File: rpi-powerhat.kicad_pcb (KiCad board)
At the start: 2 copper layers, 65 x 56 mm, 5 parts, among them J2 rpi-gpio-powerhat

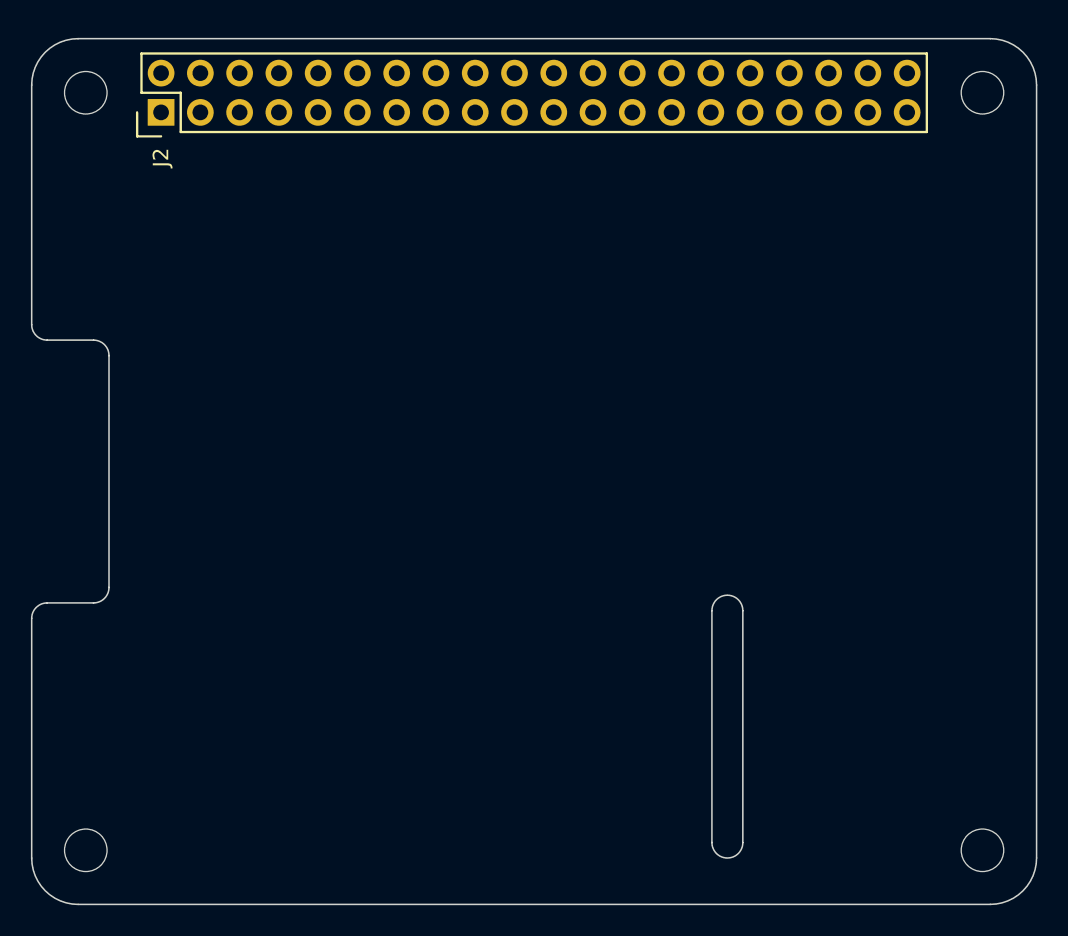
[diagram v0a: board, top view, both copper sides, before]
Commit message: Made the powerhat even smaller
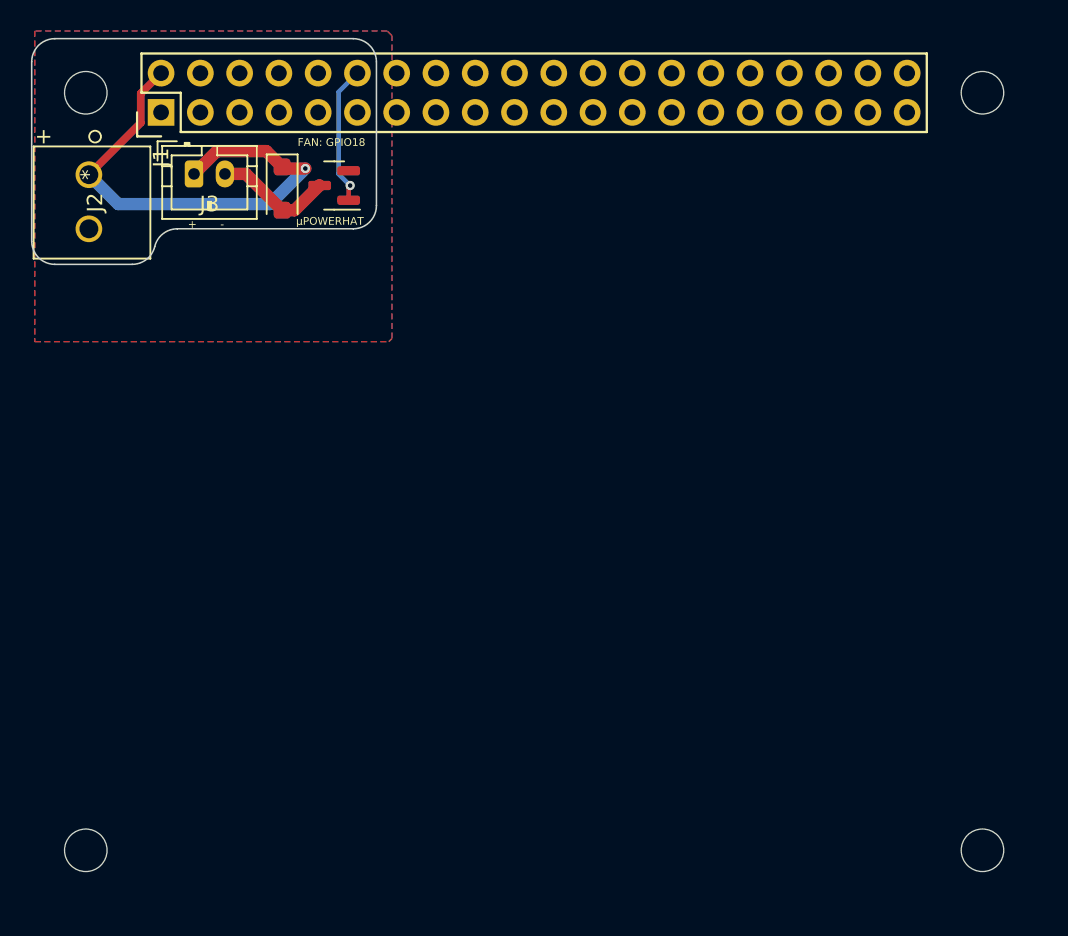
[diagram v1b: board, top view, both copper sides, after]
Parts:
- added D1: D, Diode_SMD:D_SOD-123F, F.Cu at (16.2, 10.2)
- added J2: +5V, rpi-powerhat:1546551-2, F.Cu at (3.70, 9.30)
- added J3: FAN, Connector_JST:JST_PH_B2B-PH-K_1x02_P2.00mm_Vertical, F.Cu at (10.5, 9.25)
- added Q2: AO3402, Package_TO_SOT_SMD:SOT-23, F.Cu at (19.6, 10.0)
- J1: renamed from J2; footprint RPi_Hat:Pin_Header_Straight_2x20 -> rpi-powerhat:Pin_Header_Straight_2x20
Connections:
- J1 pad 1: Net-(J2-Pad1) -> unconnected-(J1-3.3V-Pad1)
- J1 pad 10: Net-(J2-Pad10) -> unconnected-(J1-BCM15_RXD-Pad10)
- J1 pad 11: Net-(J2-Pad11) -> unconnected-(J1-BCM17-Pad11)
- J1 pad 12: Net-(J2-Pad12) -> GPIO18
- J1 pad 13: Net-(J2-Pad13) -> unconnected-(J1-BCM27-Pad13)
- J1 pad 14: Net-(J2-Pad14) -> unconnected-(J1-GND-Pad14)
- J1 pad 15: Net-(J2-Pad15) -> unconnected-(J1-BCM22-Pad15)
- J1 pad 16: Net-(J2-Pad16) -> unconnected-(J1-BCM23-Pad16)
- J1 pad 17: Net-(J2-Pad17) -> unconnected-(J1-3.3V-Pad17)
- J1 pad 18: Net-(J2-Pad18) -> unconnected-(J1-BCM24-Pad18)
- J1 pad 19: Net-(J2-Pad19) -> unconnected-(J1-BCM10_MOSI-Pad19)
- J1 pad 2: Net-(J2-Pad2) -> +5V
- J1 pad 20: Net-(J2-Pad20) -> unconnected-(J1-GND-Pad20)
- J1 pad 21: Net-(J2-Pad21) -> unconnected-(J1-BCM9_MISO-Pad21)
- J1 pad 22: Net-(J2-Pad22) -> unconnected-(J1-BCM25-Pad22)
- J1 pad 23: Net-(J2-Pad23) -> unconnected-(J1-BCM11_SCLK-Pad23)
- J1 pad 24: Net-(J2-Pad24) -> unconnected-(J1-BCM8_CE0-Pad24)
- J1 pad 25: Net-(J2-Pad25) -> unconnected-(J1-GND-Pad25)
- J1 pad 26: Net-(J2-Pad26) -> unconnected-(J1-BCM7_CE1-Pad26)
- J1 pad 27: Net-(J2-Pad27) -> unconnected-(J1-BCM0_ID_SD-Pad27)
- J1 pad 28: Net-(J2-Pad28) -> unconnected-(J1-BCM1_ID_SC-Pad28)
- J1 pad 29: Net-(J2-Pad29) -> unconnected-(J1-BCM5-Pad29)
- J1 pad 3: Net-(J2-Pad3) -> unconnected-(J1-BCM2_SDA-Pad3)
- J1 pad 30: Net-(J2-Pad30) -> unconnected-(J1-GND-Pad30)
- J1 pad 31: Net-(J2-Pad31) -> unconnected-(J1-BCM6-Pad31)
- J1 pad 32: Net-(J2-Pad32) -> unconnected-(J1-BCM12_PWM0-Pad32)
- J1 pad 33: Net-(J2-Pad33) -> unconnected-(J1-BCM13_PWM1-Pad33)
- J1 pad 34: Net-(J2-Pad34) -> unconnected-(J1-GND-Pad34)
- J1 pad 35: Net-(J2-Pad35) -> unconnected-(J1-BCM19_MISO_PCM_FS-Pad35)
- J1 pad 36: Net-(J2-Pad36) -> unconnected-(J1-BCM16-Pad36)
- J1 pad 37: Net-(J2-Pad37) -> unconnected-(J1-BCM26-Pad37)
- J1 pad 38: Net-(J2-Pad38) -> unconnected-(J1-BCM20_MOSI_PCM_DI-Pad38)
- J1 pad 39: Net-(J2-Pad39) -> unconnected-(J1-GND-Pad39)
- J1 pad 4: Net-(J2-Pad4) -> unconnected-(J1-5V-Pad4)
- J1 pad 40: Net-(J2-Pad40) -> unconnected-(J1-BCM21_SCLK_PCM_DO-Pad40)
- J1 pad 5: Net-(J2-Pad5) -> unconnected-(J1-BCM3_SCL-Pad5)
- J1 pad 6: Net-(J2-Pad6) -> unconnected-(J1-GND-Pad6)
- J1 pad 7: Net-(J2-Pad7) -> unconnected-(J1-BCM4_GPCLK0-Pad7)
- J1 pad 8: Net-(J2-Pad8) -> unconnected-(J1-BCM14_TXD-Pad8)
- J1 pad 9: Net-(J2-Pad9) -> GND
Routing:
- net +5V: track 0.00 -> 32.5 mm, vias 0 -> 1
- net GPIO18: track 0.00 -> 9.07 mm, vias 0 -> 1
- net /rpi-gpio-powerhat/GPIO18-: track 0.00 -> 7.70 mm
- added copper zone on B.Cu, net GND
- added copper zone on F.Cu, net GND
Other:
- board size 65 x 56 mm -> 22.3 x 14.6 mm
- board text added: "+"
- board text added: "-"
- board text added: "FAN: GPIO18"
- board text added: "GND"
- board text added: "µPOWERHAT"
- board text removed: "Camera Flex Slot (Optional)"

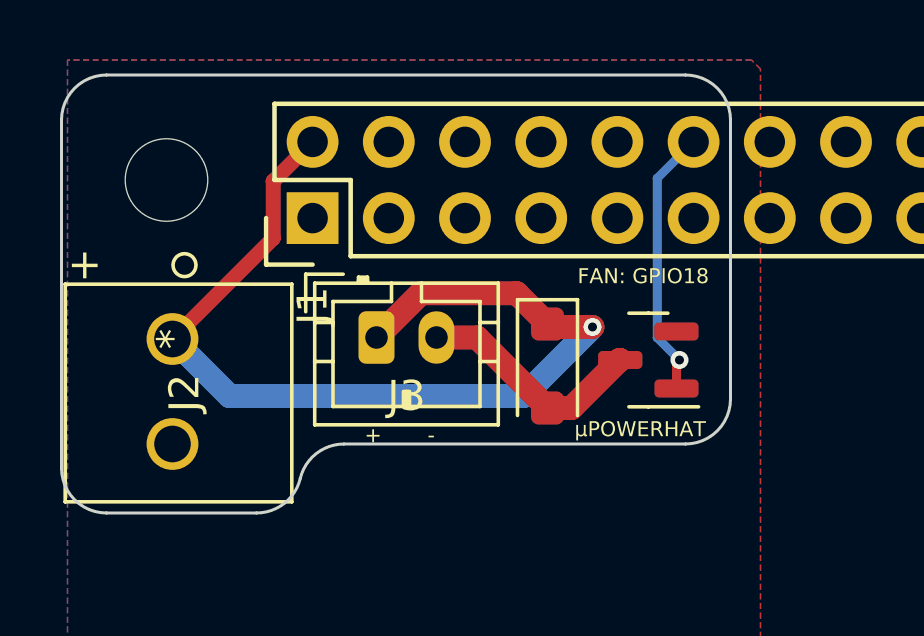
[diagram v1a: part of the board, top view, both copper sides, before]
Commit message: Added more vias
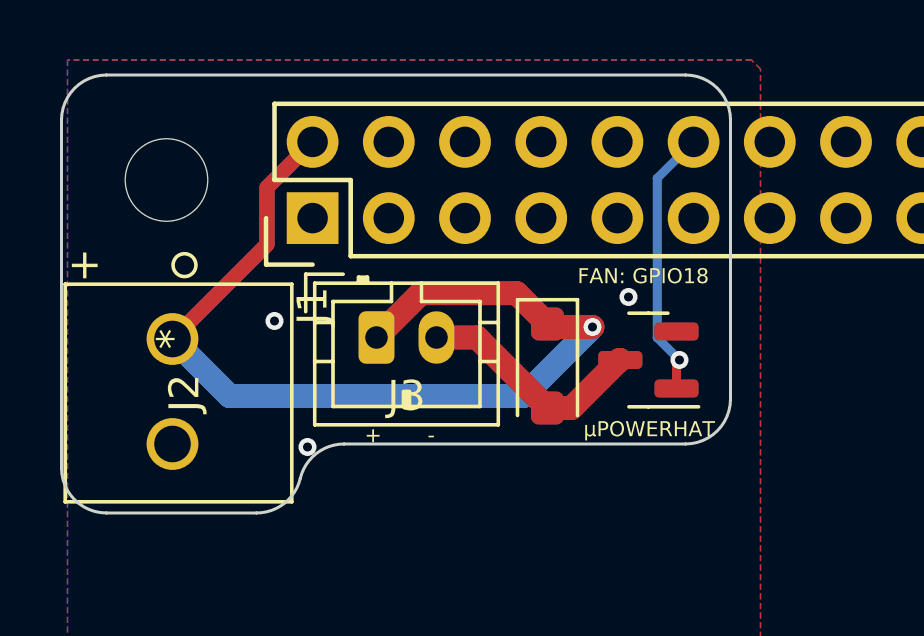
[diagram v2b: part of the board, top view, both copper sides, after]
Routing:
- net +5V: track 32.5 -> 41.0 mm
- net GND: vias 0 -> 3
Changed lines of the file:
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@@
     (effects (font (size 0.5 0.5) (thickness 0.125)) (justify left bottom))
   )
-  (gr_text "µPOWERHAT" (at 17.1 12.6) (layer "F.SilkS")
+  (gr_text "µPOWERHAT" (at 17.4 12.6) (layer "F.SilkS")
     (effects (font (size 0.5 0.5) (thickness 0.125)) (justify left bottom))
   )
@@
   (segment (start 17.7 8.9) (end 16.3 8.9) (width 0.8) (layer "F.Cu") (net 3))
   (segment (start 16.3 8.9) (end 16.2 8.8) (width 0.8) (layer "F.Cu") (net 3))
-  (segment (start 7.0564 5.9436) (end 3.7 9.3) (width 0.5) (layer "F.Cu") (net 3))
   (segment (start 11.975 7.775) (end 10.5 9.25) (width 0.8) (layer "F.Cu") (net 3))
-  (segment (start 8.37 2.73) (end 7.0564 4.0436) (width 0.5) (layer "F.Cu") (net 3))
+  (segment (start 6.85 6.15) (end 3.7 9.3) (width 0.5) (layer "F.Cu") (net 3))
+  (segment (start 6.85 4.25) (end 6.85 6.15) (width 0.5) (layer "F.Cu") (net 3))
   (segment (start 15.175 7.775) (end 11.975 7.775) (width 0.8) (layer "F.Cu") (net 3))
   (segment (start 16.2 8.8) (end 15.175 7.775) (width 0.8) (layer "F.Cu") (net 3))
-  (segment (start 7.0564 4.0436) (end 7.0564 5.9436) (width 0.5) (layer "F.Cu") (net 3))
+  (segment (start 8.37 2.73) (end 6.85 4.25) (width 0.5) (layer "F.Cu") (net 3))
   (via (at 17.7 8.9) (size 0.6) (drill 0.3) (layers "F.Cu" "B.Cu") (net 3))
   (segment (start 17.7 8.9) (end 15.4 11.2) (width 0.8) (layer "B.Cu") (net 3))
   (segment (start 15.4 11.2) (end 5.6 11.2) (width 0.8) (layer "B.Cu") (net 3))
+  (segment (start 3.7 9.3) (end 6.85 6.15) (width 0.5) (layer "B.Cu") (net 3))
+  (segment (start 6.85 6.15) (end 6.85 4.25) (width 0.5) (layer "B.Cu") (net 3))
+  (segment (start 6.85 4.25) (end 8.37 2.73) (width 0.5) (layer "B.Cu") (net 3))
   (segment (start 5.6 11.2) (end 3.7 9.3) (width 0.8) (layer "B.Cu") (net 3))
+  (via (at 7.1 8.7) (size 0.6) (drill 0.3) (layers "F.Cu" "B.Cu") (free) (net 5))
+  (via (at 8.2 12.9) (size 0.6) (drill 0.3) (layers "F.Cu" "B.Cu") (free) (net 5))
+  (via (at 18.9 7.9) (size 0.6) (drill 0.3) (layers "F.Cu" "B.Cu") (free) (net 5))
   (segment (start 18.6 10) (end 17 11.6) (width 0.8) (layer "F.Cu") (net 39))
   (segment (start 13.85 9.25) (end 12.714214 9.25) (width 0.8) (layer "F.Cu") (net 39))

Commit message: Added recent changes and production files
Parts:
- removed the ? at (61.5, 4.00)
- removed the ? at (3.50, 53.0)
- removed the ? at (61.5, 53.0)
- J1: footprint rpi-powerhat:Pin_Header_Straight_2x20 -> Connector_PinHeader_2.54mm:PinHeader_2x06_P2.54mm_Vertical
- J2: value +5V -> VIN
- moved J1 24.2 mm to (8.37, 5.27)
